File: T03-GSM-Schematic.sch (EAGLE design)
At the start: 20 parts, among them J1 POWER_JACKPTH_BREAD, J2 AVR_SPI_PRG_62X3_LOCK, Q2 16M, U1 ATMEGA328P-PU, U2 LM317MDT-TR

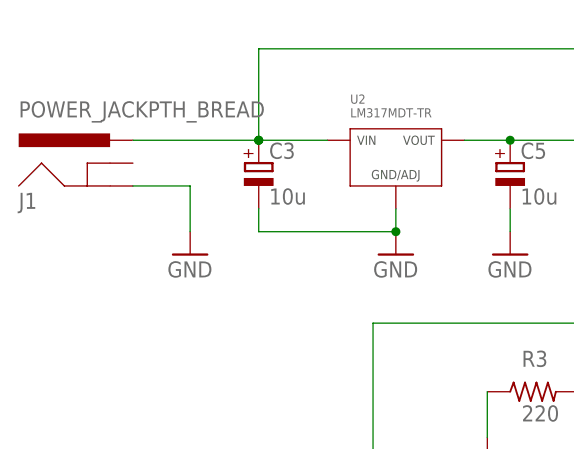
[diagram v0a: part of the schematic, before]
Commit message: Switched power + and - on power jack
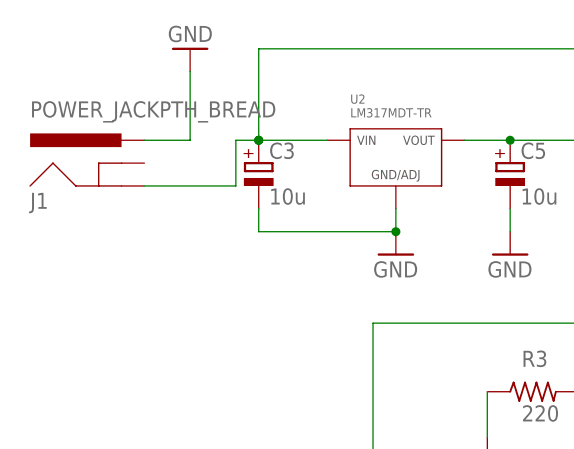
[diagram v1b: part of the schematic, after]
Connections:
- net 12V: now also J1.GND; no longer J1.PWR
- net GND: now also J1.PWR; no longer J1.GND
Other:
- moved on the sheet: J1
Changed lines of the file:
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@@
 <setting verticaltext="up"/>
 </settings>
-<grid distance="0.1" unitdist="inch" unit="inch" style="lines" multiple="1" display="no" altdistance="0.01" altunitdist="inch" altunit="inch"/>
+<grid distance="0.1" unitdist="inch" unit="inch" style="lines" multiple="1" display="yes" altdistance="0.01" altunitdist="inch" altunit="inch"/>
 <layers>
 <layer number="1" name="Top" color="4" fill="1" visible="no" active="no"/>
@@
 </instance>
 <instance part="GND6" gate="1" x="190.5" y="86.36"/>
-<instance part="J1" gate="G$1" x="143.51" y="198.12"/>
-<instance part="GND7" gate="1" x="152.4" y="193.04"/>
+<instance part="J1" gate="G$1" x="144.78" y="198.12"/>
+<instance part="GND7" gate="1" x="152.4" y="215.9" rot="R180"/>
 <instance part="FRAME1" gate="G$1" x="0" y="0"/>
 <instance part="FRAME1" gate="G$2" x="325.12" y="0"/>
@@
 </segment>
 <segment>
-<pinref part="J1" gate="G$1" pin="GND"/>
-<wire x1="146.05" y1="200.66" x2="152.4" y2="200.66" width="0.1524" layer="91"/>
-<wire x1="152.4" y1="200.66" x2="152.4" y2="195.58" width="0.1524" layer="91"/>
-<pinref part="GND7" gate="1" pin="GND"/>
-</segment>
-<segment>
 <pinref part="GND3" gate="1" pin="GND"/>
 <wire x1="187.96" y1="198.12" x2="187.96" y2="195.58" width="0.1524" layer="91"/>
@@
 <pinref part="GND5" gate="1" pin="GND"/>
 <pinref part="LED3" gate="G$1" pin="C"/>
+</segment>
+<segment>
+<pinref part="GND7" gate="1" pin="GND"/>
+<wire x1="152.4" y1="213.36" x2="152.4" y2="205.74" width="0.1524" layer="91"/>
+<wire x1="152.4" y1="205.74" x2="147.32" y2="205.74" width="0.1524" layer="91"/>
+<pinref part="J1" gate="G$1" pin="PWR"/>
 </segment>
 </net>
@@
 <wire x1="160.02" y1="205.74" x2="167.64" y2="205.74" width="0.1524" layer="91"/>
 <junction x="160.02" y="205.74"/>
-<pinref part="J1" gate="G$1" pin="PWR"/>
-<wire x1="146.05" y1="205.74" x2="160.02" y2="205.74" width="0.1524" layer="91"/>
 <wire x1="160.02" y1="205.74" x2="160.02" y2="215.9" width="0.1524" layer="91"/>
 <junction x="160.02" y="205.74"/>
@@
 <wire x1="284.48" y1="142.24" x2="276.86" y2="142.24" width="0.1524" layer="91"/>
 <junction x="284.48" y="142.24"/>
-</segment>
-</net>
+<wire x1="157.48" y1="200.66" x2="157.48" y2="205.74" width="0.1524" layer="91"/>
+<wire x1="157.48" y1="205.74" x2="160.02" y2="205.74" width="0.1524" layer="91"/>
+<pinref part="J1" gate="G$1" pin="GND"/>
+<wire x1="157.48" y1="200.66" x2="147.32" y2="200.66" width="0.1524" layer="91"/>
+</segment>
+</net>

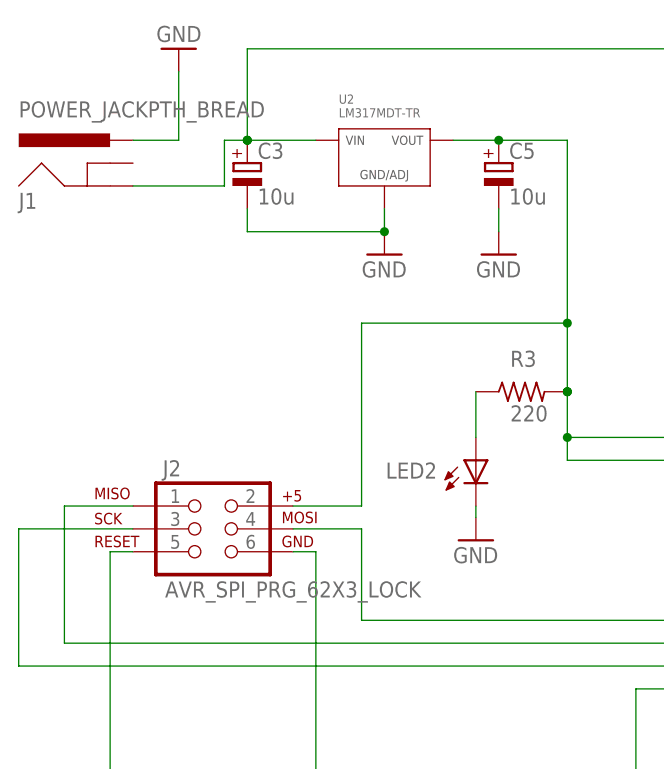
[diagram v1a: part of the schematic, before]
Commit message: Change the Voltage regulator to through hole
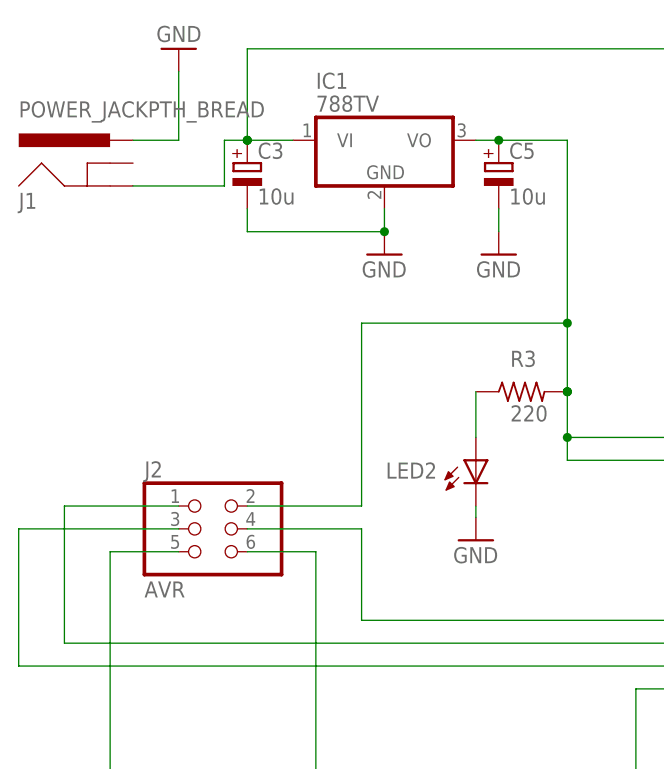
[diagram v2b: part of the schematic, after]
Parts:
- removed U2: LM317MDT-TR, MF_IC_Power:LM317MDT-TR
- added IC1: 788TV, linear:788TV
- J2: value AVR_SPI_PRG_62X3_LOCK -> AVR; device SparkFun-Connectors:AVR_SPI_PRG_62X3_LOCK -> pinhead:PINHD-2X3
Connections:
- net 12V: now also IC1.VI; no longer U2.VIN
- net 5V: now also IC1.VO; no longer U2.VOUT
- net GND: now also IC1.GND; no longer U2.GND/ADJ
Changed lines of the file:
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@@
 <?xml version="1.0" encoding="utf-8"?>
 <!DOCTYPE eagle SYSTEM "eagle.dtd">
-<eagle version="7.7.0">
+<eagle version="7.5.0">
 <drawing>
 <settings>
@@
 <setting verticaltext="up"/>
 </settings>
-<grid distance="0.1" unitdist="inch" unit="inch" style="lines" multiple="1" display="yes" altdistance="0.01" altunitdist="inch" altunit="inch"/>
+<grid distance="0.1" unitdist="inch" unit="inch" style="lines" multiple="1" display="no" altdistance="0.01" altunitdist="inch" altunit="inch"/>
 <layers>
 <layer number="1" name="Top" color="4" fill="1" visible="no" active="no"/>
@@
 <part name="C5" library="rcl" deviceset="CPOL-EU" device="E5-10.5" value="10u"/>
 <part name="LED3" library="led" deviceset="LED" device="5MM"/>
-<part name="U2" library="MF_IC_Power" deviceset="LM317" device="MDT-TR" value="LM317MDT-TR"/>
 <part name="D1" library="diode" deviceset="1N4004" device=""/>
-<part name="J2" library="SparkFun-Connectors" deviceset="AVR_SPI_PRG_6" device="2X3_LOCK"/>
+<part name="J2" library="pinhead" deviceset="PINHD-2X3" device="" value="AVR"/>
+<part name="IC1" library="linear" deviceset="78*" device="TV" technology="8" value="788TV"/>
 </parts>
 <sheets>
@@
 <instance part="C5" gate="G$1" x="187.96" y="203.2"/>
 <instance part="LED3" gate="G$1" x="295.91" y="149.86" rot="R90"/>
-<instance part="U2" gate="G$1" x="170.18" y="205.74"/>
 <instance part="D1" gate="1" x="284.48" y="139.7" smashed="yes" rot="R270">
 <attribute name="NAME" x="279.4" y="138.9126" size="1.778" layer="95"/>
 <attribute name="VALUE" x="280.67" y="133.5786" size="1.778" layer="96"/>
 </instance>
-<instance part="J2" gate="G$1" x="154.94" y="162.56"/>
+<instance part="J2" gate="A" x="154.94" y="162.56"/>
+<instance part="IC1" gate="A1" x="175.26" y="205.74"/>
 </instances>
 <busses>
@@
 <junction x="175.26" y="195.58"/>
 <pinref part="C3" gate="G$1" pin="-"/>
-<pinref part="U2" gate="G$1" pin="GND/ADJ"/>
+<pinref part="IC1" gate="A1" pin="GND"/>
 </segment>
 <segment>
@@
 <wire x1="218.44" y1="134.62" x2="218.44" y2="130.81" width="0.1524" layer="91"/>
 <wire x1="167.64" y1="134.62" x2="218.44" y2="134.62" width="0.1524" layer="91"/>
-<wire x1="165.1" y1="160.02" x2="167.64" y2="160.02" width="0.1524" layer="91"/>
+<wire x1="160.02" y1="160.02" x2="167.64" y2="160.02" width="0.1524" layer="91"/>
 <wire x1="167.64" y1="160.02" x2="167.64" y2="134.62" width="0.1524" layer="91"/>
-<pinref part="J2" gate="G$1" pin="6"/>
+<pinref part="J2" gate="A" pin="6"/>
 </segment>
 <segment>
@@
 <net name="N$7" class="0">
 <segment>
-<wire x1="165.1" y1="162.56" x2="172.72" y2="162.56" width="0.1524" layer="91"/>
+<wire x1="160.02" y1="162.56" x2="172.72" y2="162.56" width="0.1524" layer="91"/>
 <wire x1="172.72" y1="162.56" x2="172.72" y2="152.4" width="0.1524" layer="91"/>
 <wire x1="172.72" y1="152.4" x2="218.44" y2="152.4" width="0.1524" layer="91"/>
 <pinref part="U1" gate="A" pin="PB3"/>
-<pinref part="J2" gate="G$1" pin="4"/>
+<pinref part="J2" gate="A" pin="4"/>
 </segment>
 </net>
@@
 <wire x1="139.7" y1="149.86" x2="218.44" y2="149.86" width="0.1524" layer="91"/>
 <pinref part="U1" gate="A" pin="PB4"/>
-<wire x1="147.32" y1="165.1" x2="139.7" y2="165.1" width="0.1524" layer="91"/>
+<wire x1="152.4" y1="165.1" x2="139.7" y2="165.1" width="0.1524" layer="91"/>
 <wire x1="139.7" y1="165.1" x2="139.7" y2="149.86" width="0.1524" layer="91"/>
-<pinref part="J2" gate="G$1" pin="1"/>
+<pinref part="J2" gate="A" pin="1"/>
 </segment>
 </net>
@@
 <wire x1="173.99" y1="124.46" x2="254" y2="124.46" width="0.1524" layer="91"/>
 <wire x1="254" y1="124.46" x2="254" y2="134.62" width="0.1524" layer="91"/>
-<wire x1="147.32" y1="160.02" x2="144.78" y2="160.02" width="0.1524" layer="91"/>
+<wire x1="152.4" y1="160.02" x2="144.78" y2="160.02" width="0.1524" layer="91"/>
 <wire x1="144.78" y1="160.02" x2="144.78" y2="124.46" width="0.1524" layer="91"/>
 <pinref part="R1" gate="G$1" pin="2"/>
 <junction x="173.99" y="124.46"/>
-<pinref part="J2" gate="G$1" pin="5"/>
+<pinref part="J2" gate="A" pin="5"/>
 </segment>
 </net>
@@
 <wire x1="215.9" y1="170.18" x2="195.58" y2="170.18" width="0.1524" layer="91"/>
 <wire x1="172.72" y1="185.42" x2="195.58" y2="185.42" width="0.1524" layer="91"/>
-<wire x1="165.1" y1="165.1" x2="172.72" y2="165.1" width="0.1524" layer="91"/>
+<wire x1="160.02" y1="165.1" x2="172.72" y2="165.1" width="0.1524" layer="91"/>
 <wire x1="172.72" y1="165.1" x2="172.72" y2="185.42" width="0.1524" layer="91"/>
 <pinref part="U1" gate="A" pin="AREF"/>
@@
 <wire x1="218.44" y1="172.72" x2="195.58" y2="172.72" width="0.1524" layer="91"/>
 <junction x="195.58" y="172.72"/>
-<pinref part="U2" gate="G$1" pin="VOUT"/>
-<wire x1="182.88" y1="205.74" x2="187.96" y2="205.74" width="0.1524" layer="91"/>
-<pinref part="J2" gate="G$1" pin="2"/>
+<pinref part="J2" gate="A" pin="2"/>
+<pinref part="IC1" gate="A1" pin="VO"/>
+<wire x1="185.42" y1="205.74" x2="187.96" y2="205.74" width="0.1524" layer="91"/>
 </segment>
 </net>
@@
 <net name="12V" class="0">
 <segment>
-<wire x1="160.02" y1="205.74" x2="167.64" y2="205.74" width="0.1524" layer="91"/>
+<wire x1="160.02" y1="205.74" x2="165.1" y2="205.74" width="0.1524" layer="91"/>
 <junction x="160.02" y="205.74"/>
 <wire x1="160.02" y1="205.74" x2="160.02" y2="215.9" width="0.1524" layer="91"/>
@@
 <junction x="276.86" y="142.24"/>
 <pinref part="C3" gate="G$1" pin="+"/>
-<pinref part="U2" gate="G$1" pin="VIN"/>
 <pinref part="D1" gate="1" pin="A"/>
 <wire x1="284.48" y1="142.24" x2="276.86" y2="142.24" width="0.1524" layer="91"/>
@@
 <pinref part="J1" gate="G$1" pin="GND"/>
 <wire x1="157.48" y1="200.66" x2="147.32" y2="200.66" width="0.1524" layer="91"/>
+<pinref part="IC1" gate="A1" pin="VI"/>
 </segment>
 </net>
@@
 <segment>
 <pinref part="U1" gate="A" pin="PB5"/>
-<wire x1="147.32" y1="162.56" x2="134.62" y2="162.56" width="0.1524" layer="91"/>
+<wire x1="152.4" y1="162.56" x2="134.62" y2="162.56" width="0.1524" layer="91"/>
 <wire x1="134.62" y1="162.56" x2="134.62" y2="147.32" width="0.1524" layer="91"/>
 <wire x1="218.44" y1="147.32" x2="134.62" y2="147.32" width="0.1524" layer="91"/>
-<pinref part="J2" gate="G$1" pin="3"/>
-</segment>
-</net>
+<pinref part="J2" gate="A" pin="3"/>
+</segment>
+</net>

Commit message: Added terminal points for GSM module
5V and GND
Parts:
- removed RX, TX: (no value), wirepad:2,54/0,9
- added SV1: GSM-header, con-lstb:MA04-1
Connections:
- removed net N$1: TX.P, U1.PD2
- removed net N$12: RX.P, U1.PD3
- new net RX: SV1.4, U1.PD3
- new net TX: SV1.3, U1.PD2
- net 5V: now also SV1.2
- net GND: now also SV1.1
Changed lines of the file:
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@@
 <?xml version="1.0" encoding="utf-8"?>
 <!DOCTYPE eagle SYSTEM "eagle.dtd">
-<eagle version="7.5.0">
+<eagle version="7.7.0">
 <drawing>
 <settings>
@@
 <part name="R1" library="rcl" deviceset="R-US_" device="R0603" value="10k"/>
 <part name="LED2" library="led" deviceset="LED" device="SML0603"/>
-<part name="TX" library="wirepad" deviceset="2,54/0,9" device=""/>
-<part name="RX" library="wirepad" deviceset="2,54/0,9" device=""/>
 <part name="GND8" library="supply1" deviceset="GND" device=""/>
 <part name="GND9" library="supply1" deviceset="GND" device=""/>
@@
 <part name="J2" library="pinhead" deviceset="PINHD-2X3" device="" value="AVR"/>
 <part name="IC1" library="linear" deviceset="78*" device="TV" technology="8" value="788TV"/>
+<part name="SV1" library="con-lstb" deviceset="MA04-1" device="" value="GSM-header"/>
+<part name="GND12" library="supply1" deviceset="GND" device=""/>
 </parts>
 <sheets>
@@
 <attribute name="VALUE" x="191.135" y="165.608" size="1.778" layer="96" rot="R90"/>
 </instance>
-<instance part="TX" gate="1" x="264.16" y="167.64" smashed="yes" rot="R180">
-<attribute name="NAME" x="265.303" y="170.8658" size="1.778" layer="95" rot="R180"/>
-<attribute name="VALUE" x="265.303" y="170.942" size="1.778" layer="96" rot="R180"/>
-</instance>
-<instance part="RX" gate="1" x="264.16" y="165.1" smashed="yes" rot="R180">
-<attribute name="NAME" x="265.303" y="163.2458" size="1.778" layer="95" rot="R180"/>
-<attribute name="VALUE" x="265.303" y="168.402" size="1.778" layer="96" rot="R180"/>
-</instance>
 <instance part="GND8" gate="1" x="259.08" y="124.46"/>
 <instance part="GND9" gate="1" x="276.86" y="124.46"/>
@@
 <instance part="J2" gate="A" x="154.94" y="162.56"/>
 <instance part="IC1" gate="A1" x="175.26" y="205.74"/>
+<instance part="SV1" gate="1" x="269.24" y="167.64" rot="R180"/>
+<instance part="GND12" gate="1" x="261.62" y="182.88" rot="R180"/>
 </instances>
 <busses>
@@
 <pinref part="J1" gate="G$1" pin="PWR"/>
 </segment>
+<segment>
+<pinref part="SV1" gate="1" pin="1"/>
+<wire x1="261.62" y1="172.72" x2="261.62" y2="180.34" width="0.1524" layer="91"/>
+<pinref part="GND12" gate="1" pin="GND"/>
+</segment>
 </net>
 <net name="N$3" class="0">
@@
 <segment>
 <wire x1="187.96" y1="205.74" x2="195.58" y2="205.74" width="0.1524" layer="91"/>
-<wire x1="195.58" y1="205.74" x2="195.58" y2="185.42" width="0.1524" layer="91"/>
+<wire x1="195.58" y1="205.74" x2="195.58" y2="193.04" width="0.1524" layer="91"/>
+<wire x1="195.58" y1="193.04" x2="195.58" y2="185.42" width="0.1524" layer="91"/>
 <wire x1="195.58" y1="185.42" x2="195.58" y2="177.8" width="0.1524" layer="91"/>
 <wire x1="195.58" y1="170.18" x2="195.58" y2="172.72" width="0.1524" layer="91"/>
@@
 <pinref part="IC1" gate="A1" pin="VO"/>
 <wire x1="185.42" y1="205.74" x2="187.96" y2="205.74" width="0.1524" layer="91"/>
-</segment>
-</net>
-<net name="N$1" class="0">
+<pinref part="SV1" gate="1" pin="2"/>
+<wire x1="256.54" y1="193.04" x2="256.54" y2="170.18" width="0.1524" layer="91"/>
+<wire x1="256.54" y1="170.18" x2="261.62" y2="170.18" width="0.1524" layer="91"/>
+<wire x1="256.54" y1="193.04" x2="195.58" y2="193.04" width="0.1524" layer="91"/>
+<junction x="195.58" y="193.04"/>
+</segment>
+</net>
+<net name="TX" class="0">
 <segment>
 <pinref part="U1" gate="A" pin="PD2"/>
-<pinref part="TX" gate="1" pin="P"/>
 <wire x1="261.62" y1="167.64" x2="254" y2="167.64" width="0.1524" layer="91"/>
-</segment>
-</net>
-<net name="N$12" class="0">
+<pinref part="SV1" gate="1" pin="3"/>
+</segment>
+</net>
+<net name="RX" class="0">
 <segment>
 <pinref part="U1" gate="A" pin="PD3"/>
-<pinref part="RX" gate="1" pin="P"/>
 <wire x1="261.62" y1="165.1" x2="254" y2="165.1" width="0.1524" layer="91"/>
-</segment>
-</net>
+<pinref part="SV1" gate="1" pin="4"/>
+</segment>
+</net>
